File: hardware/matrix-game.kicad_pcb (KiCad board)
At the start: 2 copper layers, 100 x 100 mm, 32 parts, among them SW1 button_center, SW2 button_left, SW3 button_down, SW4 button_right, SW5 button_up, U1 NUCLEO-F042K6, U2 MAX7219, U3 DM-OLED096-636

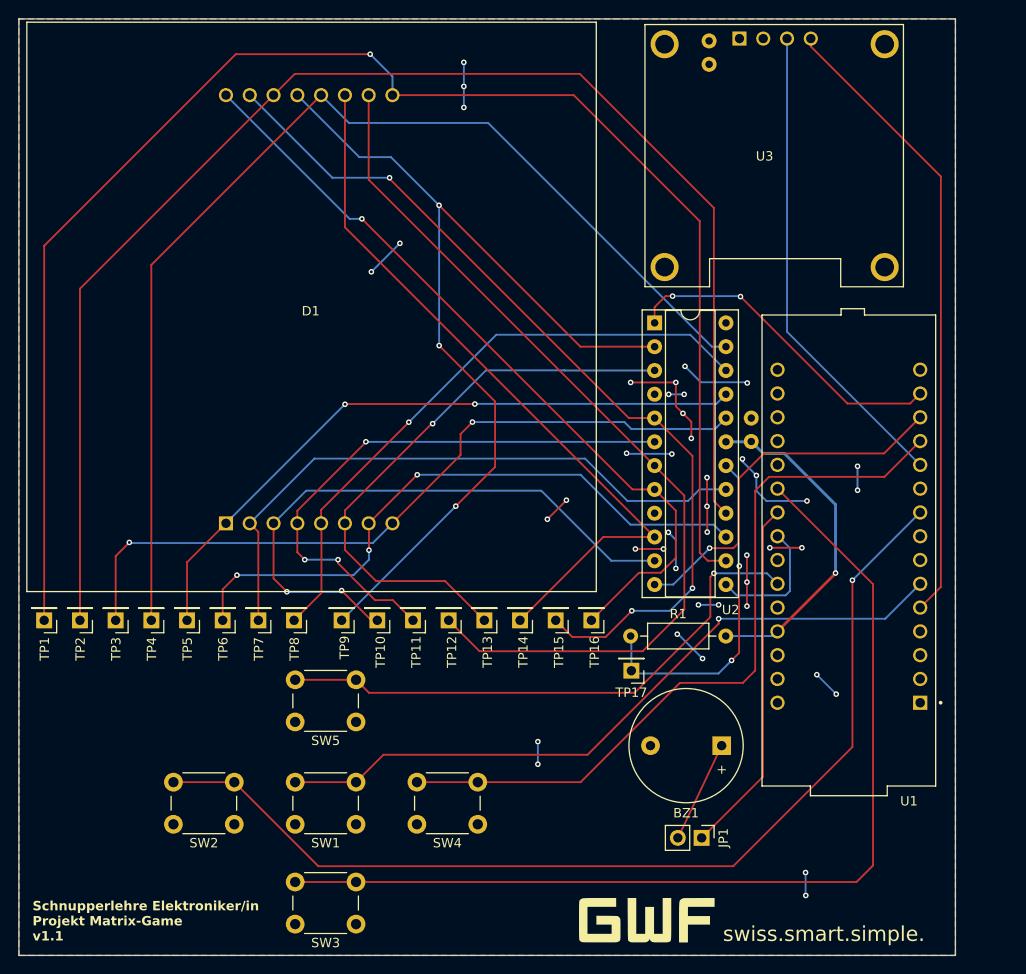
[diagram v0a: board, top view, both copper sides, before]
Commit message: [Hardware] Replaced old pin headers with new 1x16, 2.54mm pin headers
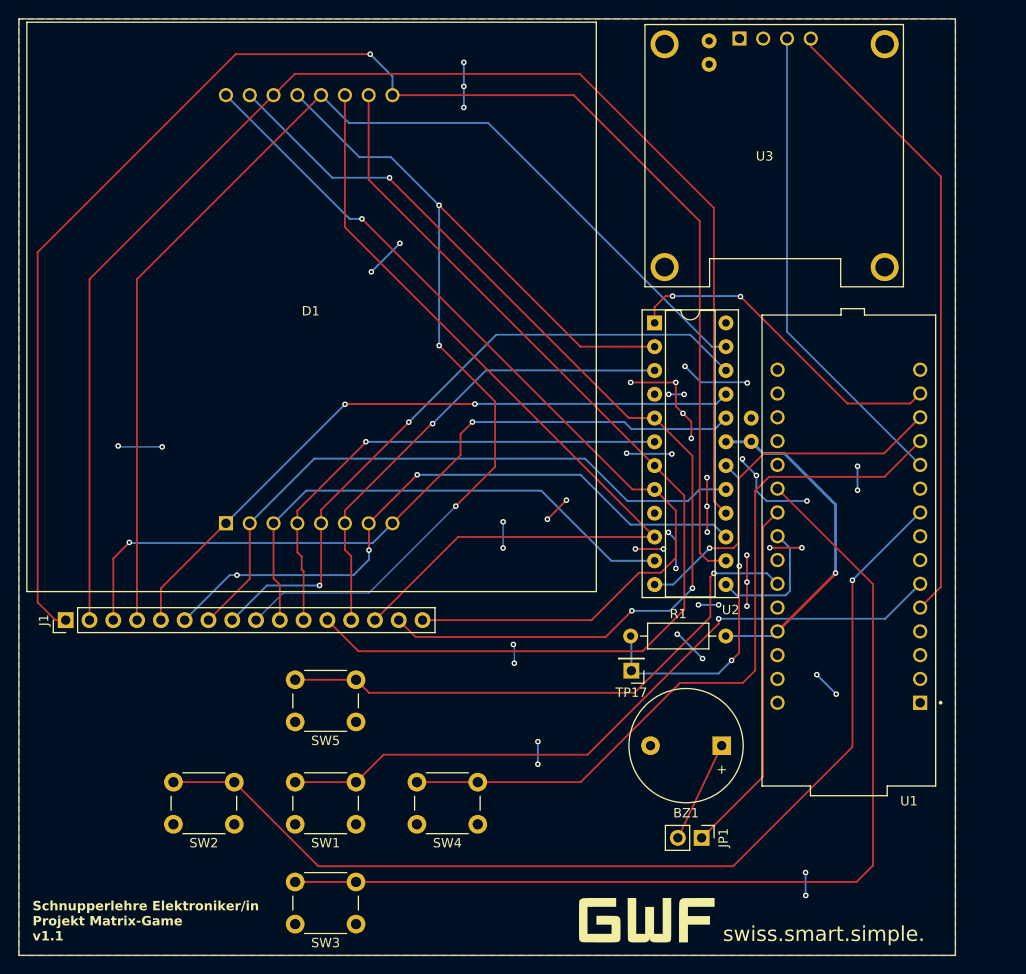
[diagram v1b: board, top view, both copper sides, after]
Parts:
- removed TP1, TP10, TP11, TP12, TP13, TP14, TP15, TP16, TP2, TP3, TP4, TP5, TP6, TP7, TP8, TP9: TestPoint, Connector_PinHeader_2.54mm:PinHeader_1x01_P2.54mm_Vertical
- added J1: Conn_01x16_Pin, Connector_PinHeader_2.54mm:PinHeader_1x16_P2.54mm_Vertical, F.Cu at (95.0, 109.2)
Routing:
- net Net-(D1-C8): track 83.2 -> 101.3 mm
- net Net-(D1-C7): track 95.0 -> 111.7 mm
- net Net-(D1-C6): track 78.9 -> 94.4 mm
- net Net-(D1-C4): track 97.3 -> 110.2 mm
- net Net-(D1-C5): track 61.5 -> 51.3 mm
- net GND: track 53.5 -> 63.1 mm, vias 28 -> 34
- net Net-(D1-C1): track 102.9 -> 112.0 mm
- net Net-(D1-C2): track 64.2 -> 55.9 mm, vias 2 -> 0
- net Net-(D1-C3): track 61.3 -> 53.2 mm, vias 3 -> 1
- net Net-(D1-R8): track 65.6 -> 72.0 mm, vias 1 -> 2
- net Net-(D1-R1): track 165.6 -> 167.7 mm
- net Net-(D1-R6): track 67.2 -> 69.3 mm
- net Net-(D1-R7): track 66.8 -> 68.3 mm
- net Net-(D1-R5): track 71.2 -> 72.3 mm
- net Net-(D1-R4): track 117.9 -> 118.6 mm

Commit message: tbs
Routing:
- net GND: track 63.1 -> 80.4 mm, vias 34 -> 42
- net +3.3V: track 32.1 -> 36.5 mm, vias 16 -> 20
- net Net-(D1-R6): vias 3 -> 2
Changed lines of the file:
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@@
 		)
 		(fp_text user "${REFERENCE}"
-			(at 0 19.05 360)
+			(at 0 19.05 0)
 			(layer "F.Fab")
 			(effects
@@
 	)
 	(via
+		(at 115.9 102.7)
+		(size 0.6)
+		(drill 0.3)
+		(layers "F.Cu" "B.Cu")
+		(net 1)
+	)
+	(via
 		(at 160.15 103.675)
 		(size 0.6)
@@
 	)
 	(via
+		(at 113.2 102.7)
+		(size 0.6)
+		(drill 0.3)
+		(layers "F.Cu" "B.Cu")
+		(net 1)
+	)
+	(via
 		(at 174.15 96.475)
 		(size 0.6)
@@
 		(drill 0.3)
 		(layers "F.Cu" "B.Cu")
+		(free yes)
 		(net 1)
 	)
@@
 	)
 	(via
+		(at 123.6 102.7)
+		(size 0.6)
+		(drill 0.3)
+		(layers "F.Cu" "B.Cu")
+		(net 1)
+	)
+	(via
 		(at 145.415 124.587)
 		(size 0.6)
@@
 	)
 	(via
+		(at 107.9 105.2)
+		(size 0.6)
+		(drill 0.3)
+		(layers "F.Cu" "B.Cu")
+		(net 1)
+	)
+	(via
 		(at 154.89 91.38)
 		(size 0.6)
@@
 	)
 	(via
+		(at 101.6 104)
+		(size 0.6)
+		(drill 0.3)
+		(layers "F.Cu" "B.Cu")
+		(net 1)
+	)
+	(via
+		(at 118.5 102.7)
+		(size 0.6)
+		(drill 0.3)
+		(layers "F.Cu" "B.Cu")
+		(net 1)
+	)
+	(via
 		(at 161.125 82.1)
 		(size 0.6)
@@
 	)
 	(via
+		(at 121.3 102.7)
+		(size 0.6)
+		(drill 0.3)
+		(layers "F.Cu" "B.Cu")
+		(net 1)
+	)
+	(via
 		(at 141.7 98.7)
 		(size 0.6)
@@
 	)
 	(via
+		(at 104 104)
+		(size 0.6)
+		(drill 0.3)
+		(layers "F.Cu" "B.Cu")
+		(free yes)
+		(net 1)
+	)
+	(via
 		(at 127.635 72.009)
 		(size 0.6)
@@
 	)
 	(segment
+		(start 101.7 104.1)
+		(end 103.9 104.1)
+		(width 0.127)
+		(layer "B.Cu")
+		(net 1)
+	)
+	(segment
+		(start 101.6 104)
+		(end 101.7 104.1)
+		(width 0.127)
+		(layer "B.Cu")
+		(net 1)
+	)
+	(segment
 		(start 163 113.3)
 		(end 160.4 110.7)
@@
 	)
 	(segment
+		(start 121.3 102.7)
+		(end 118.5 102.7)
+		(width 0.127)
+		(layer "B.Cu")
+		(net 1)
+	)
+	(segment
 		(start 137.51 54.46)
 		(end 137.51 52.21)
@@
 	)
 	(segment
+		(start 123.6 102.7)
+		(end 121.3 102.7)
+		(width 0.127)
+		(layer "B.Cu")
+		(net 1)
+	)
+	(segment
 		(start 142.9 111.9)
 		(end 142.8 111.8)
@@
 	)
 	(segment
+		(start 118.5 102.7)
+		(end 115.9 102.7)
+		(width 0.127)
+		(layer "B.Cu")
+		(net 1)
+	)
+	(segment
 		(start 174 136.15)
 		(end 174 138.575)
@@
 	)
 	(segment
+		(start 113.2 102.7)
+		(end 115.9 102.7)
+		(width 0.127)
+		(layer "B.Cu")
+		(net 1)
+	)
+	(segment
 		(start 154.89 91.38)
 		(end 154.95 91.44)
@@
 	)
 	(segment
+		(start 107.9 105.2)
+		(end 105.2 105.2)
+		(width 0.127)
+		(layer "B.Cu")
+		(net 1)
+	)
+	(segment
 		(start 167.26 91.98)
 		(end 167.26 92.26)
@@
 	)
 	(segment
+		(start 105.2 105.2)
+		(end 104 104)
+		(width 0.127)
+		(layer "B.Cu")
+		(net 1)
+	)
+	(segment
 		(start 162.825 83.8)
 		(end 161.125 82.1)
@@
 	)
 	(segment
+		(start 103.9 104.1)
+		(end 104 104)
+		(width 0.127)
+		(layer "B.Cu")
+		(net 1)
+	)
+	(segment
 		(start 127.635 72.009)
 		(end 127.762 72.009)
@@
 	)
 	(via
-		(at 113.284 104.394)
-		(size 0.6)
-		(drill 0.3)
-		(layers "F.Cu" "B.Cu")
-		(net 8)
-	)
-	(via
 		(at 127.381 101.727)
 		(size 0.6)
@@
 	)
 	(segment
+		(start 124.8 103.5)
+		(end 123.9 104.4)
+		(width 0.127)
+		(layer "F.Cu")
+		(net 19)
+	)
+	(segment
 		(start 161.798 89.789)
 		(end 161.798 88.011)
@@
 	)
 	(segment
+		(start 123.9 104.4)
+		(end 123.9 105.4)
+		(width 0.127)
+		(layer "F.Cu")
+		(net 19)
+	)
+	(segment
+		(start 112.5 105.5)
+		(end 111.3 105.5)
+		(width 0.127)
+		(layer "F.Cu")
+		(net 19)
+	)
+	(segment
 		(start 167.74 102.27)
 		(end 167.73 102.26)
@@
 	)
 	(segment
+		(start 111.3 105.5)
+		(end 110.6 104.8)
+		(width 0.127)
+		(layer "F.Cu")
+		(net 19)
+	)
+	(segment
 		(start 163.475 93.975)
 		(end 163.475 97.05)
@@
 	)
 	(via
+		(at 110.6 104.8)
+		(size 0.6)
+		(drill 0.3)
+		(layers "F.Cu" "B.Cu")
+		(free yes)
+		(net 19)
+	)
+	(via
 		(at 155.829 101.6)
 		(size 0.6)
@@
 	)
 	(via
+		(at 123.9 105.4)
+		(size 0.6)
+		(drill 0.3)
+		(layers "F.Cu" "B.Cu")
+		(free yes)
+		(net 19)
+	)
+	(via
 		(at 161.798 89.789)
 		(size 0.6)
@@
 	)
 	(via
+		(at 112.5 105.5)
+		(size 0.6)
+		(drill 0.3)
+		(layers "F.Cu" "B.Cu")
+		(net 19)
+	)
+	(via
 		(at 163.475 93.975)
 		(size 0.6)
@@
 		(net 19)
 	)
+	(via
+		(at 124.8 103.5)
+		(size 0.6)
+		(drill 0.3)
+		(layers "F.Cu" "B.Cu")
+		(net 19)
+	)

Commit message: [firmware/doc] updated changelog
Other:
- board text added: "Schnupperlehre Elektroniker/in Projekt Matrix-Game v1.2"
- board text removed: "Schnupperlehre Elektroniker/in Projekt Matrix-Game v1.1"
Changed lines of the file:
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@@
 		(layer "Edge.Cuts")
 	)
-	(gr_text "Schnupperlehre Elektroniker/in\nProjekt Matrix-Game\nv1.1"
+	(gr_text "Schnupperlehre Elektroniker/in\nProjekt Matrix-Game\nv1.2"
 		(at 91.45 143.525 0)
 		(layer "F.SilkS")
